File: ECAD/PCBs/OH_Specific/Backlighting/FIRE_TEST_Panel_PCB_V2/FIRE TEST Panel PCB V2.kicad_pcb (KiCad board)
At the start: 2 copper layers, 52.1 x 46.8 mm, 23 parts, among them J1 Conn_01x04_Female, J2 Conn_01x04_Female

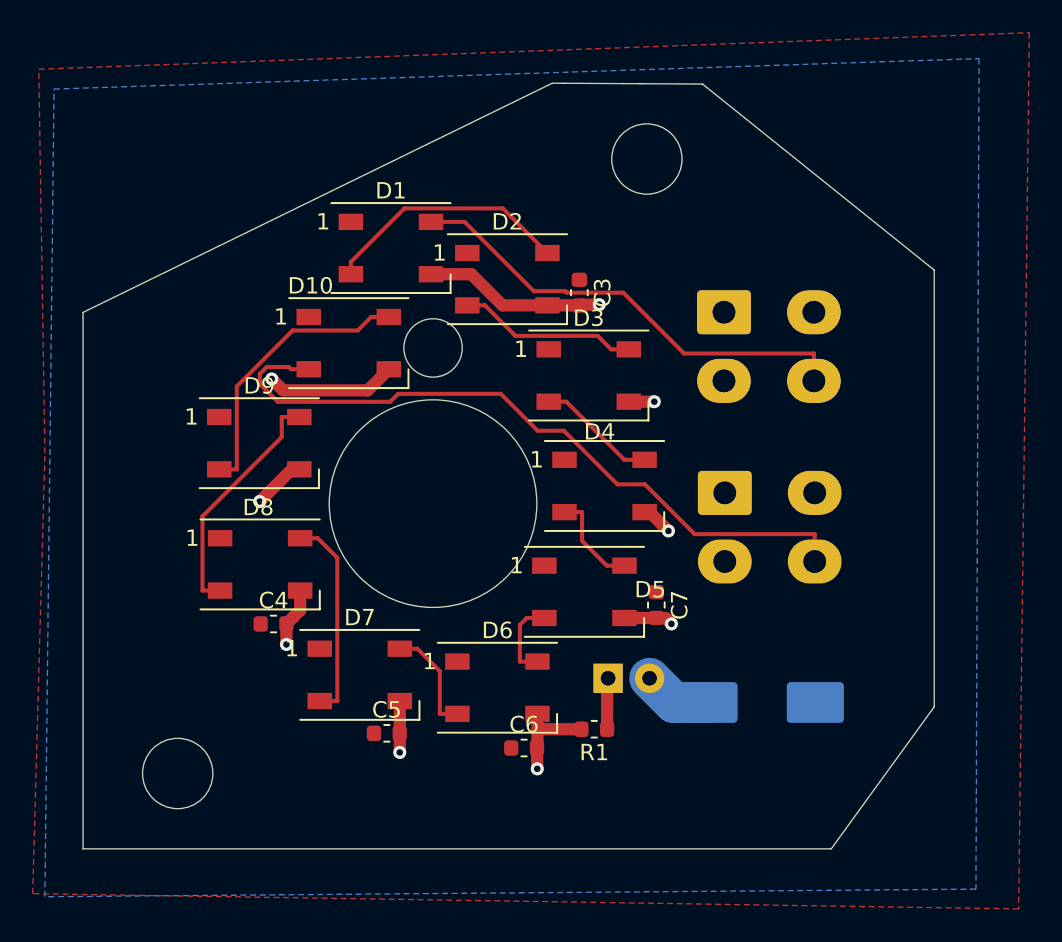
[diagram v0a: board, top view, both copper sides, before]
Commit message: Fire Test Panel Backlighting Updates
Changed - Front copper fill from solid to thermal relief.
Changed - Tidied dirty auto routing traces
Changed - Silkscreen version to 2.1
Changed - Manufacturing files to match changes.
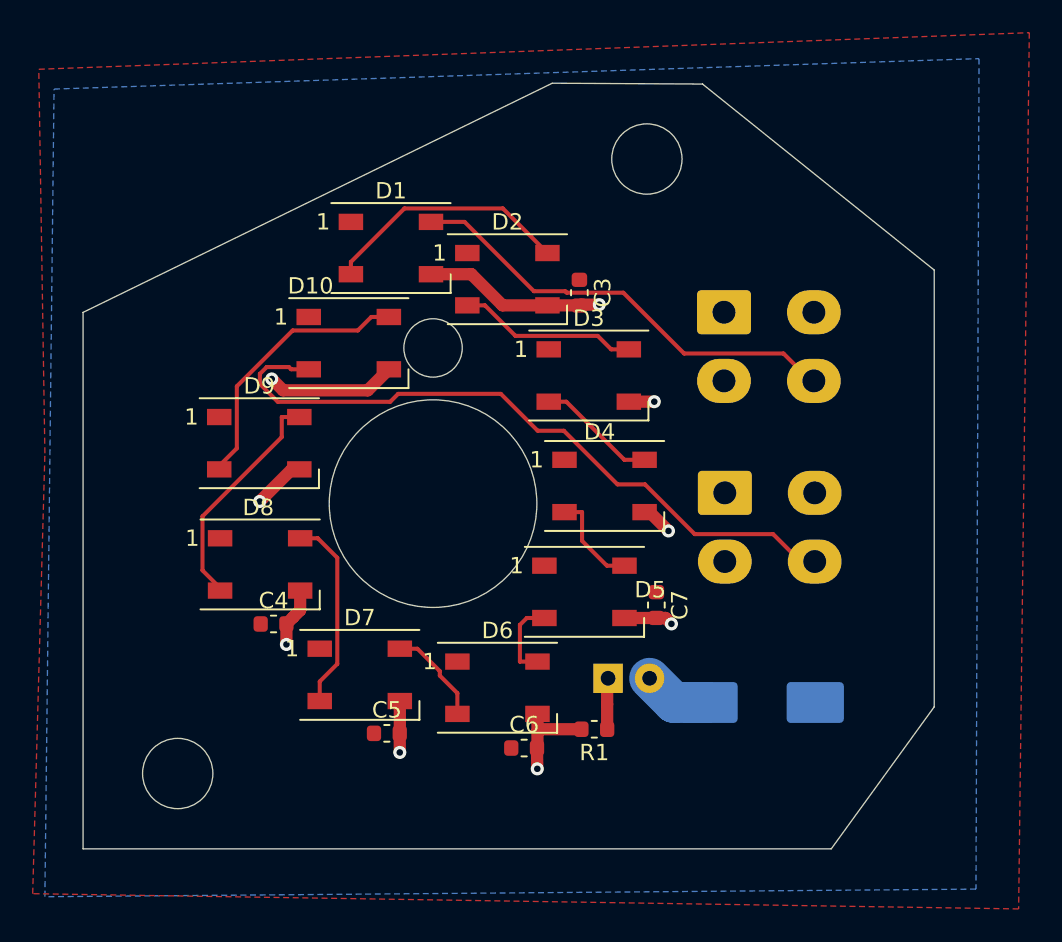
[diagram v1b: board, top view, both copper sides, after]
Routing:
- net /DATAOUT: track 43.7 -> 42.7 mm
- net /DATAIN: track 28.4 -> 27.5 mm
- net Net-(D7-Pad2): track 12.6 -> 12.0 mm
- net Net-(D6-Pad2): track 6.71 -> 6.08 mm
- net Net-(D10-Pad4): track 17.2 -> 16.6 mm
- net Net-(D8-Pad2): track 14.8 -> 14.1 mm
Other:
- board text added: "Version 2.1"
- board text removed: "Version 2.0"
